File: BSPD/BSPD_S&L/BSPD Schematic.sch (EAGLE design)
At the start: 8 parts, among them U1(AND)2CH SN74LVC2G08DCUT, U2(COMPARATOR)2CH TLV3202AIDGK

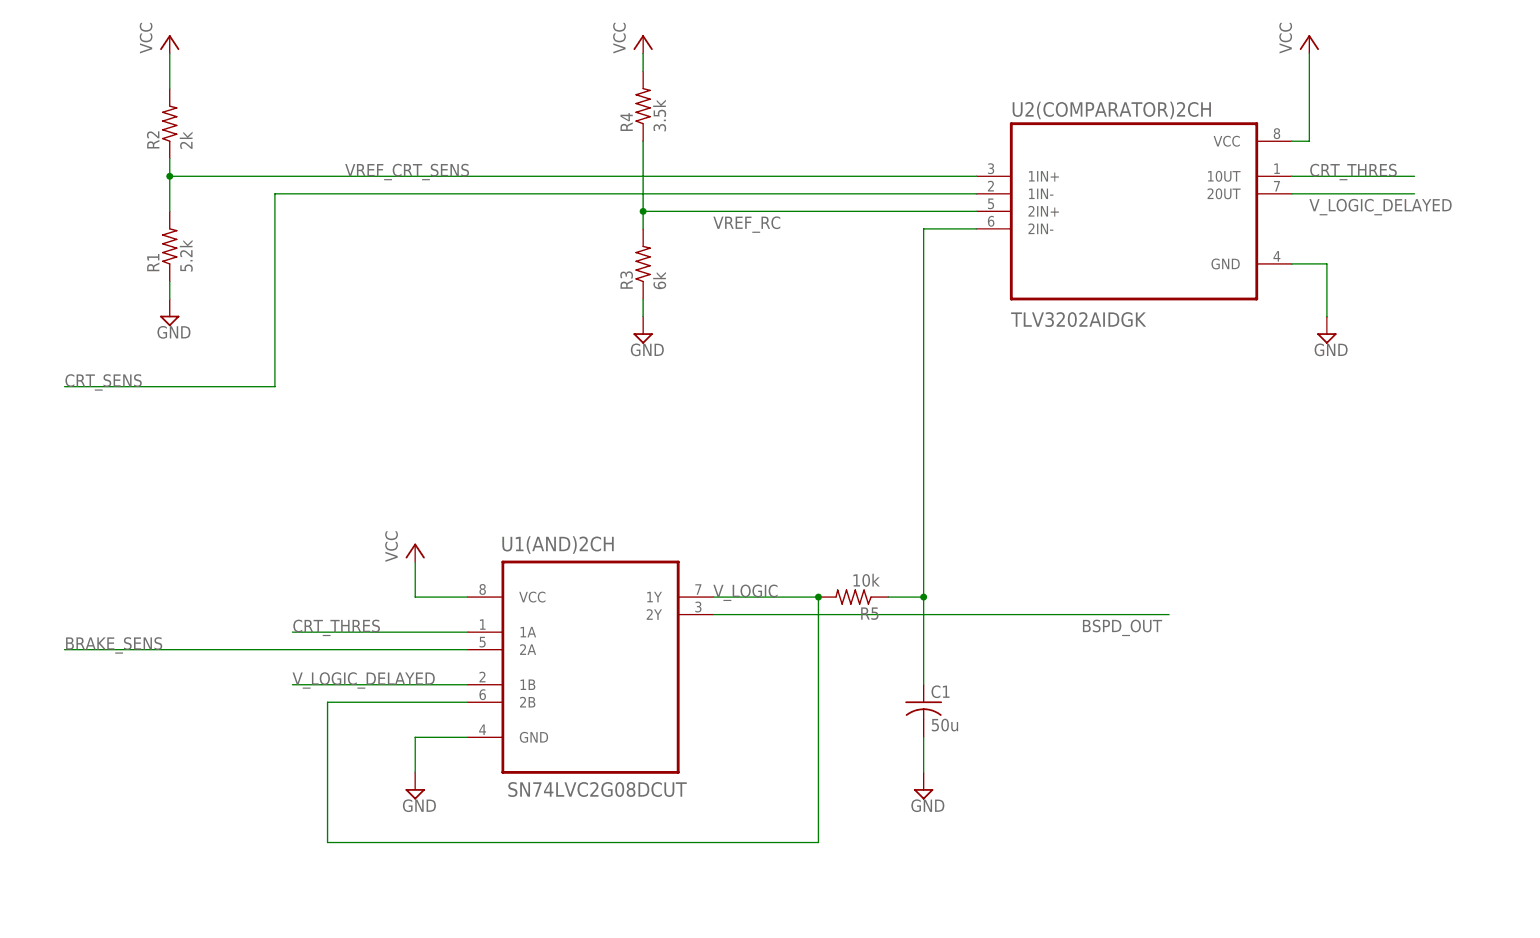
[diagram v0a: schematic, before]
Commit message: Added discharge path for capacitor
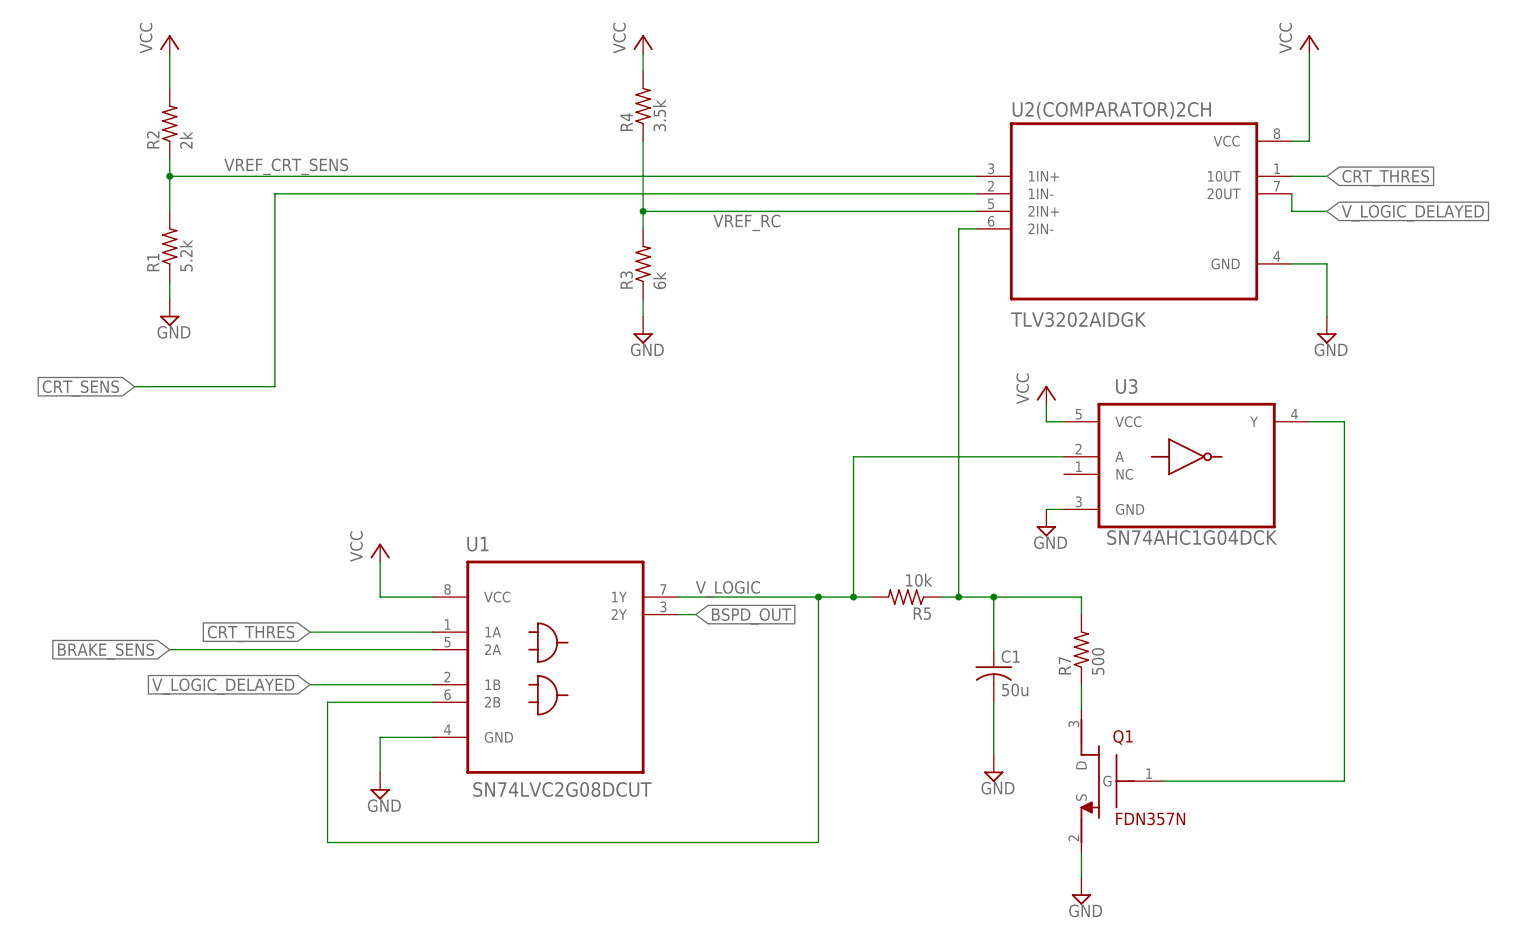
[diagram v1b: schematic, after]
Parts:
- removed U1(AND)2CH: SN74LVC2G08DCUT, SN74LVC2G08DCUT:SN74LVC2G08DCUT
- added Q1: FDN357N, SOT95P280X130-3N:FDN357N
- added R7: 500, resistor:R-US_R0603
- added U1: SN74LVC2G08DCUT, SN74LVC2G08DCUT:SN74LVC2G08DCUT
- added U3: SN74AHC1G04DCK, SN74AHC1G04DCK:SN74AHC1G04DCK
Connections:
- new net N$2: Q1.D, R7.1
- new net N$3: Q1.G, U3.Y
- net BRAKE_SENS: now also U1.2A; no longer U1(AND)2CH.2A
- net BSPD_OUT: now also U1.2Y; no longer U1(AND)2CH.2Y
- net CRT_THRES: now also U1.1A; no longer U1(AND)2CH.1A
- net GND: now also Q1.S, U1.GND, U3.GND; no longer U1(AND)2CH.GND
- net N$1: now also R7.2
- net VCC: now also U1.VCC, U3.VCC; no longer U1(AND)2CH.VCC
- net V_LOGIC: now also U1.1Y, U1.2B, U3.A; no longer U1(AND)2CH.1Y, U1(AND)2CH.2B
- net V_LOGIC_DELAYED: now also U1.1B; no longer U1(AND)2CH.1B
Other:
- moved on the sheet: C1, R5
